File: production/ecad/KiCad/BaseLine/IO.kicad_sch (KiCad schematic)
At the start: 0 parts

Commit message: Added level shifter to load cell
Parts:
- added U12: CD74HC4067M96, CD74HC4067M96:SOIC127P1030X265-24N, symbol CD74HC4067M96:CD74HC4067M96
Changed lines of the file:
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@@
 	(generator_version "8.0")
 	(paper "A4")
+	(symbol
+		(lib_id "CD74HC4067M96:CD74HC4067M96")
+		(at 137.16 82.55 0)
+		(unit 1)
+		(exclude_from_sim no)
+		(in_bom yes)
+		(on_board yes)
+		(dnp no)
+		(fields_autoplaced yes)
+		(property "Reference" "U12"
+			(at 137.16 49.53 0)
+			(effects
+				(font
+					(size 1.27 1.27)
+				)
+			)
+		)
+		(property "Value" "CD74HC4067M96"
+			(at 137.16 52.07 0)
+			(effects
+				(font
+					(size 1.27 1.27)
+				)
+			)
+		)
+		(property "Footprint" "CD74HC4067M96:SOIC127P1030X265-24N"
+			(at 137.16 82.55 0)
+			(effects
+				(font
+					(size 1.27 1.27)
+				)
+				(justify bottom)
+				(hide yes)
+			)
+		)
+		(property "Datasheet" "https://www.digikey.com/en/products/detail/texas-instruments/CD74HC4067M96/1507236"
+			(at 137.16 82.55 0)
+			(effects
+				(font
+					(size 1.27 1.27)
+				)
+				(hide yes)
+			)
+		)
+		(property "Description" ""
+			(at 137.16 82.55 0)
+			(effects
+				(font
+					(size 1.27 1.27)
+				)
+				(hide yes)
+			)
+		)
+		(pin "2"
+		)
+		(pin "9"
+		)
+		(pin "5"
+		)
+		(pin "12"
+		)
+		(pin "16"
+		)
+		(pin "17"
+		)
+		(pin "19"
+		)
+		(pin "7"
+		)
+		(pin "8"
+		)
+		(pin "3"
+		)
+		(pin "10"
+		)
+		(pin "18"
+		)
+		(pin "1"
+		)
+		(pin "15"
+		)
+		(pin "13"
+		)
+		(pin "23"
+		)
+		(pin "22"
+		)
+		(pin "11"
+		)
+		(pin "14"
+		)
+		(pin "6"
+		)
+		(pin "20"
+		)
+		(pin "4"
+		)
+		(pin "21"
+		)
+		(pin "24"
+		)
+		(instances
+			(project "BaseLine"
+				(path "/ba9eda21-3882-41e1-8265-3d8ac781da20/e3080f39-1d26-4bce-b471-534f477eeea5"
+					(reference "U12")
+					(unit 1)
+				)
+			)
+		)
+	)
 )

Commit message: Update IO.kicad_sch
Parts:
- added J10: Conn_LoadCell1, symbol Connector:Conn_01x04_Socket
- added J11: Conn_LoadCell2, symbol Connector:Conn_01x04_Socket
- added J12: Conn_LoadCell3, symbol Connector:Conn_01x04_Socket
- added J13: Conn_LoadCell4, symbol Connector:Conn_01x04_Socket
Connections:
- net MUX_CS_1: now reaches U12.10 (S0)
- net MUX_CS_2: now reaches U12.11 (S1)
- net GND: now reaches U12.12 (GND)
- net MUX_CS_4: now reaches U12.13 (S3)
- net MUX_CS_3: now reaches U12.14 (S2)
- net at U12.16 (I15): now also J13.4 (Pin_4)
- net at U12.17 (I14): now also J13.3 (Pin_3)
- net at U12.18 (I13): now also J13.2 (Pin_2)
- net at U12.19 (I12): now also J13.1 (Pin_1)
- net at U12.2 (I7): now also J11.4 (Pin_4)
- net at U12.20 (I11): now also J12.4 (Pin_4)
- net at U12.21 (I10): now also J12.3 (Pin_3)
- net at U12.22 (I9): now also J12.2 (Pin_2)
- net at U12.23 (I8): now also J12.1 (Pin_1)
- net +5V: now reaches U12.24 (VCC)
- net at U12.3 (I6): now also J11.3 (Pin_3)
- net at U12.4 (I5): now also J11.2 (Pin_2)
- net at U12.5 (I4): now also J11.1 (Pin_1)
- net at U12.6 (I3): now also J10.4 (Pin_4)
- net at U12.7 (I2): now also J10.3 (Pin_3)
- net at U12.8 (I1): now also J10.2 (Pin_2)
- net at U12.9 (I0): now also J10.1 (Pin_1)

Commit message: Final mux changes
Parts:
- J10: value Conn_LoadCell1 -> LoadCell1
- J11: value Conn_LoadCell2 -> LoadCell2
- J12: value Conn_LoadCell3 -> LoadCell3
- J13: value Conn_LoadCell4 -> LoadCell4
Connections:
- net DATA_OUTPUT: now reaches U12.1 (COM_I/O)
- net ENABLE: now reaches U12.15 (~{E})
- net at U12.16 (I15): no longer J13.4 (Pin_4)
- net at U12.17 (I14): no longer J13.3 (Pin_3)
- net at U12.18 (I13): no longer J13.2 (Pin_2)
- net at U12.19 (I12): no longer J13.1 (Pin_1)
- net at U12.2 (I7): no longer J11.4 (Pin_4)
- net at U12.20 (I11): no longer J12.4 (Pin_4)
- net at U12.21 (I10): no longer J12.3 (Pin_3)
- net at U12.22 (I9): no longer J12.2 (Pin_2)
- net at U12.23 (I8): no longer J12.1 (Pin_1)
- net at U12.3 (I6): no longer J11.3 (Pin_3)
- net at U12.4 (I5): no longer J11.2 (Pin_2)
- net at U12.5 (I4): no longer J11.1 (Pin_1)
- net DOUT_3: now reaches U12.6 (I3)
- net DOUT_3: now also J13.1 (Pin_1); no longer J10.4 (Pin_4)
- net DOUT_2: now reaches U12.7 (I2)
- net DOUT_2: now also J12.1 (Pin_1); no longer J10.3 (Pin_3)
- net CLK: now reaches J10.2 (Pin_2)
- net CLK: now also J11.2 (Pin_2), J12.2 (Pin_2), J13.2 (Pin_2); no longer U12.8 (I1)
- net DOUT_0: now reaches J10.1 (Pin_1), U12.9 (I0)
- net MUX_CS_3: no longer names the net of U12.14 (S2)
- net MUX_CS_4: no longer names the net of U12.13 (S3)
- new net DOUT_1: J11.1 (Pin_1), U12.8 (I1)
- new net PWDN: J10.3 (Pin_3), J11.3 (Pin_3), J12.3 (Pin_3), J13.3 (Pin_3)
- new net SPEED: J10.4 (Pin_4), J11.4 (Pin_4), J12.4 (Pin_4), J13.4 (Pin_4)
- no-connect marks 0 -> 14
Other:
- moved on the sheet: U12

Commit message: Update IO.kicad_sch
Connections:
- net ENABLE renamed ENABLE_MUX
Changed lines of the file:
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@@
 		)
 	)
-	(global_label "ENABLE"
+	(global_label "ENABLE_MUX"
 		(shape input)
 		(at 127 83.82 180)
@@
 		)
 		(property "Intersheetrefs" "${INTERSHEET_REFS}"
-			(at 116.9996 83.82 0)
+			(at 112.0406 83.82 0)
 			(effects
 				(font

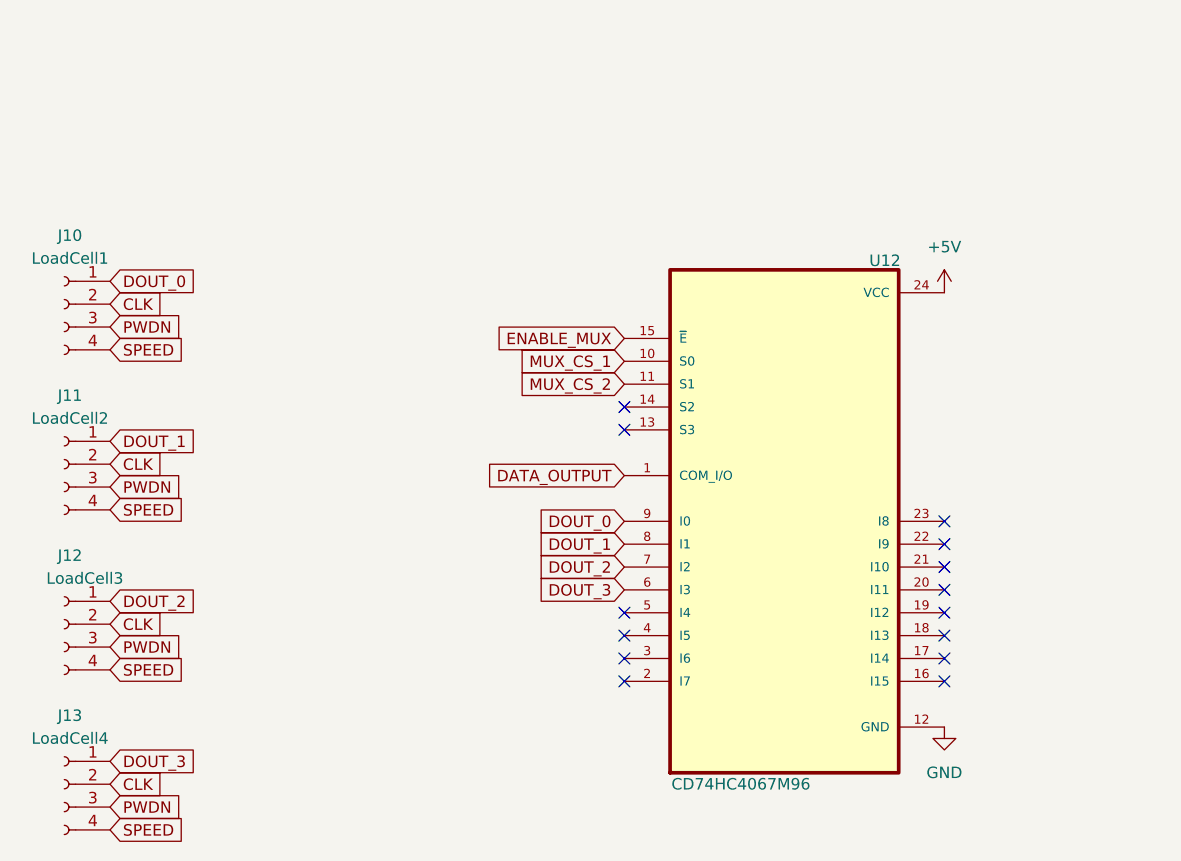
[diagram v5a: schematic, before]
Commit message: Updated more footprints
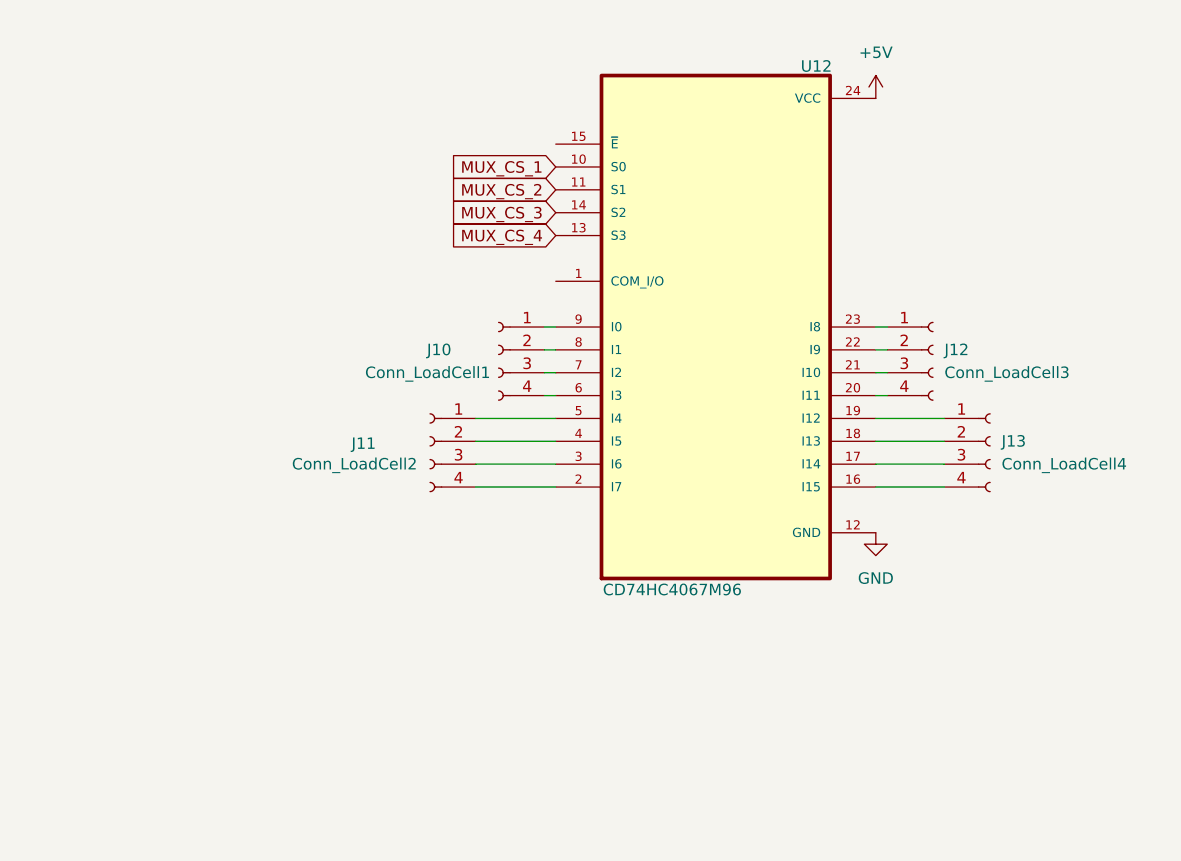
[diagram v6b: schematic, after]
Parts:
- J10: value LoadCell1 -> Conn_LoadCell1
- J11: value LoadCell2 -> Conn_LoadCell2
- J12: value LoadCell3 -> Conn_LoadCell3
- J13: value LoadCell4 -> Conn_LoadCell4
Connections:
- net MUX_CS_4: now reaches U12.13 (S3)
- net MUX_CS_3: now reaches U12.14 (S2)
- net at U12.16 (I15): now also J13.4 (Pin_4)
- net at U12.17 (I14): now also J13.3 (Pin_3)
- net at U12.18 (I13): now also J13.2 (Pin_2)
- net at U12.19 (I12): now also J13.1 (Pin_1)
- net at U12.2 (I7): now also J11.4 (Pin_4)
- net at U12.20 (I11): now also J12.4 (Pin_4)
- net at U12.21 (I10): now also J12.3 (Pin_3)
- net at U12.22 (I9): now also J12.2 (Pin_2)
- net at U12.23 (I8): now also J12.1 (Pin_1)
- net at U12.3 (I6): now also J11.3 (Pin_3)
- net at U12.4 (I5): now also J11.2 (Pin_2)
- net at U12.5 (I4): now also J11.1 (Pin_1)
- removed net CLK: J10.2 (Pin_2), J11.2 (Pin_2), J12.2 (Pin_2), J13.2 (Pin_2)
- net DATA_OUTPUT: no longer names the net of U12.1 (COM_I/O)
- net DOUT_0: no longer names the net of J10.1 (Pin_1), U12.9 (I0)
- net DOUT_1: no longer names the net of U12.8 (I1)
- net DOUT_1: now also J10.2 (Pin_2); no longer J11.1 (Pin_1)
- net DOUT_2: no longer names the net of U12.7 (I2)
- net DOUT_2: now also J10.3 (Pin_3); no longer J12.1 (Pin_1)
- net DOUT_3: no longer names the net of U12.6 (I3)
- net DOUT_3: now also J10.4 (Pin_4); no longer J13.1 (Pin_1)
- net ENABLE_MUX: no longer names the net of U12.15 (~{E})
- removed net PWDN: J10.3 (Pin_3), J11.3 (Pin_3), J12.3 (Pin_3), J13.3 (Pin_3)
- removed net SPEED: J10.4 (Pin_4), J11.4 (Pin_4), J12.4 (Pin_4), J13.4 (Pin_4)
- no-connect marks 14 -> 0
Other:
- moved on the sheet: U12
